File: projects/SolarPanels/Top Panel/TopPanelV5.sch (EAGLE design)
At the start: 41 parts

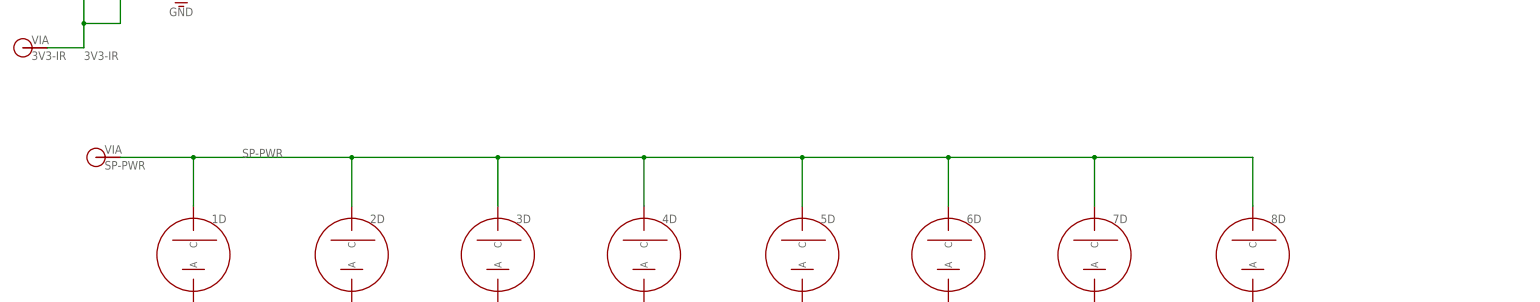
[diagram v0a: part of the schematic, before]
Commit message: Completed TopPanelV5 with new board dimensions and cells. Ready for rewview/fab
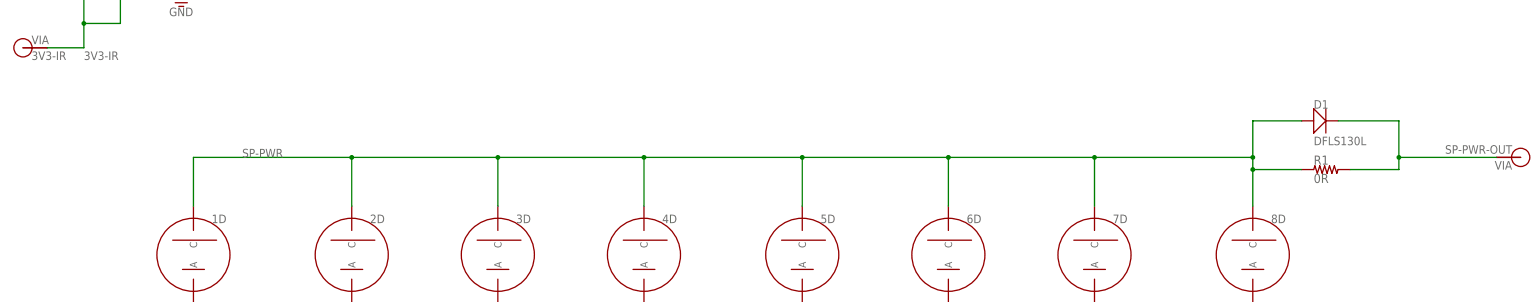
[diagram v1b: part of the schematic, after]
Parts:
- added D1: DFLS130L, BrownSpaceEngineering:DFLS130L
- added R1: 0R, BrownSpaceEngineering:RES1210
- V1: value SP-PWR -> SP-PWR-OUT
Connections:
- new net SP-PWR-OUT: D1.C, R1.2, V1.P$1
- net SP-PWR: now also D1.A, R1.1; no longer V1.P$1
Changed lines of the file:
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@@
 <part name="8B" library="BrownSpaceEngineering" deviceset="SOLARCELLV3" device=""/>
 <part name="8A" library="BrownSpaceEngineering" deviceset="SOLARCELLV3" device=""/>
-<part name="V1" library="BrownSpaceEngineering" deviceset="VIA" device="-60MIL" value="SP-PWR"/>
+<part name="V1" library="BrownSpaceEngineering" deviceset="VIA" device="-60MIL" value="SP-PWR-OUT"/>
 <part name="V4" library="BrownSpaceEngineering" deviceset="VIA" device="-60MIL" value="GND"/>
 <part name="GND1" library="supply1" deviceset="GND" device=""/>
 <part name="GND2" library="supply1" deviceset="GND" device=""/>
+<part name="D1" library="BrownSpaceEngineering" deviceset="DFLS130L" device="" value="DFLS130L"/>
+<part name="R1" library="BrownSpaceEngineering" deviceset="RES" device="1210" value="0R"/>
 </parts>
 <sheets>
@@
 <instance part="8B" gate="G$1" x="160.02" y="-38.1"/>
 <instance part="8A" gate="G$1" x="160.02" y="-63.5"/>
-<instance part="V1" gate="G$1" x="-81.28" y="33.02"/>
+<instance part="V1" gate="G$1" x="215.9" y="33.02" rot="R180"/>
 <instance part="V4" gate="G$1" x="-93.98" y="-86.36"/>
 <instance part="GND1" gate="1" x="-17.78" y="-96.52"/>
 <instance part="GND2" gate="1" x="-63.5" y="66.04"/>
+<instance part="D1" gate="G$1" x="172.72" y="40.64"/>
+<instance part="R1" gate="R$1" x="175.26" y="30.48"/>
 </instances>
 <busses>
@@
 <pinref part="8D" gate="G$1" pin="C"/>
 <wire x1="127" y1="33.02" x2="160.02" y2="33.02" width="0.1524" layer="91"/>
-<wire x1="160.02" y1="33.02" x2="160.02" y2="22.86" width="0.1524" layer="91"/>
+<wire x1="160.02" y1="33.02" x2="160.02" y2="30.48" width="0.1524" layer="91"/>
 <pinref part="7D" gate="G$1" pin="C"/>
+<wire x1="160.02" y1="30.48" x2="160.02" y2="22.86" width="0.1524" layer="91"/>
 <wire x1="96.52" y1="33.02" x2="127" y2="33.02" width="0.1524" layer="91"/>
 <wire x1="127" y1="33.02" x2="127" y2="22.86" width="0.1524" layer="91"/>
@@
 <junction x="96.52" y="33.02"/>
 <junction x="127" y="33.02"/>
-<pinref part="V1" gate="G$1" pin="P$1"/>
-<wire x1="-76.2" y1="33.02" x2="-60.96" y2="33.02" width="0.1524" layer="91"/>
-<junction x="-60.96" y="33.02"/>
+<wire x1="160.02" y1="33.02" x2="160.02" y2="40.64" width="0.1524" layer="91"/>
+<junction x="160.02" y="33.02"/>
+<pinref part="D1" gate="G$1" pin="A"/>
+<wire x1="160.02" y1="40.64" x2="170.18" y2="40.64" width="0.1524" layer="91"/>
+<pinref part="R1" gate="R$1" pin="1"/>
+<wire x1="160.02" y1="30.48" x2="170.18" y2="30.48" width="0.1524" layer="91"/>
+<junction x="160.02" y="30.48"/>
 </segment>
 </net>
@@
 </segment>
 </net>
+<net name="SP-PWR-OUT" class="0">
+<segment>
+<pinref part="R1" gate="R$1" pin="2"/>
+<wire x1="180.34" y1="30.48" x2="190.5" y2="30.48" width="0.1524" layer="91"/>
+<wire x1="190.5" y1="30.48" x2="190.5" y2="33.02" width="0.1524" layer="91"/>
+<pinref part="V1" gate="G$1" pin="P$1"/>
+<wire x1="190.5" y1="33.02" x2="210.82" y2="33.02" width="0.1524" layer="91"/>
+<pinref part="D1" gate="G$1" pin="C"/>
+<wire x1="177.8" y1="40.64" x2="190.5" y2="40.64" width="0.1524" layer="91"/>
+<wire x1="190.5" y1="40.64" x2="190.5" y2="33.02" width="0.1524" layer="91"/>
+<junction x="190.5" y="33.02"/>
+</segment>
+</net>

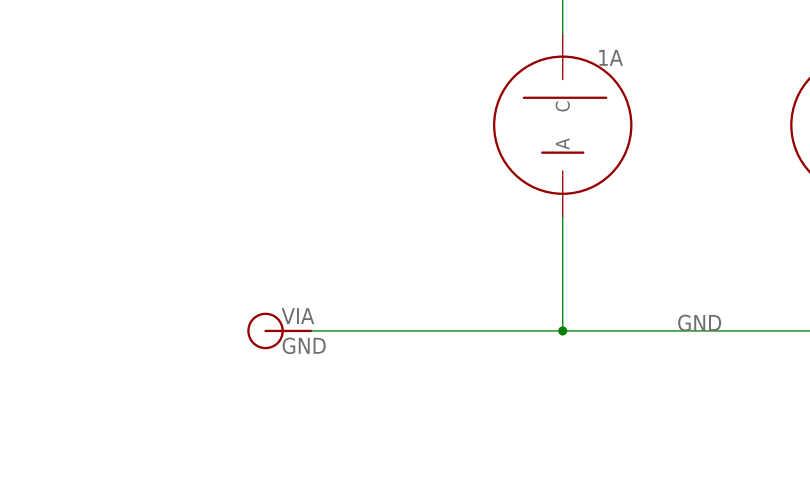
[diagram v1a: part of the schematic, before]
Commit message: Edits to TopPanelV5 per Caelan's suggestions.
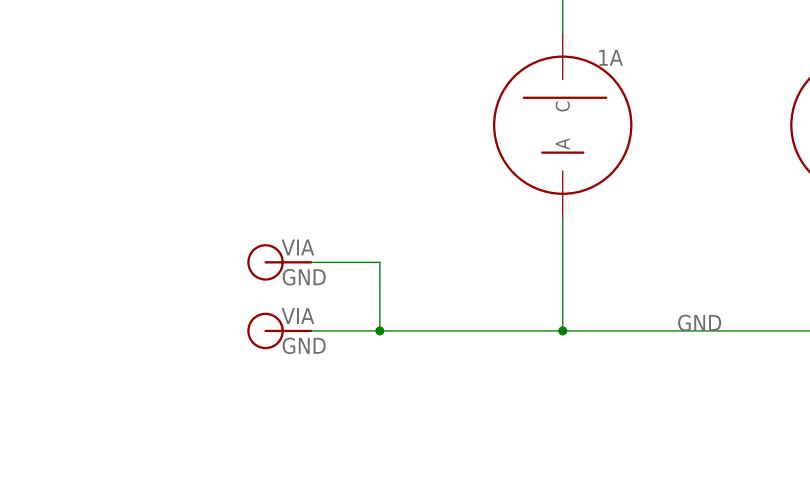
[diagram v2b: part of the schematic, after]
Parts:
- added V2: GND, BrownSpaceEngineering:VIA-60MIL
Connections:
- net GND: now also V2.P$1
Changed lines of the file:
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@@
 <part name="D1" library="BrownSpaceEngineering" deviceset="DFLS130L" device="" value="DFLS130L"/>
 <part name="R1" library="BrownSpaceEngineering" deviceset="RES" device="1210" value="0R"/>
+<part name="V2" library="BrownSpaceEngineering" deviceset="VIA" device="-60MIL" value="GND"/>
 </parts>
 <sheets>
@@
 <instance part="D1" gate="G$1" x="172.72" y="40.64"/>
 <instance part="R1" gate="R$1" x="175.26" y="30.48"/>
+<instance part="V2" gate="G$1" x="-93.98" y="-78.74"/>
 </instances>
 <busses>
@@
 <junction x="127" y="-86.36"/>
 <pinref part="V4" gate="G$1" pin="P$1"/>
-<wire x1="-88.9" y1="-86.36" x2="-60.96" y2="-86.36" width="0.1524" layer="91"/>
+<wire x1="-88.9" y1="-86.36" x2="-81.28" y2="-86.36" width="0.1524" layer="91"/>
 <junction x="-60.96" y="-86.36"/>
 <pinref part="GND1" gate="1" pin="GND"/>
+<wire x1="-81.28" y1="-86.36" x2="-60.96" y2="-86.36" width="0.1524" layer="91"/>
 <wire x1="-17.78" y1="-93.98" x2="-17.78" y2="-86.36" width="0.1524" layer="91"/>
 <junction x="-17.78" y="-86.36"/>
-</segment>
-<segment>
+<pinref part="V2" gate="G$1" pin="P$1"/>
+<wire x1="-88.9" y1="-78.74" x2="-81.28" y2="-78.74" width="0.1524" layer="91"/>
+<wire x1="-81.28" y1="-78.74" x2="-81.28" y2="-86.36" width="0.1524" layer="91"/>
+<junction x="-81.28" y="-86.36"/>
+</segment>
+<segment>
